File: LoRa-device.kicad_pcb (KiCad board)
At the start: 4 copper layers, 86.4 x 50.8 mm, 155 parts, among them J1 Micro_SD_Card_Det1, J3 Conn_01x04_Pin, J4 Conn_01x14_Pin, J6 Conn_01x04_Pin, J8 U.FL, P1 1_25T-1-2A, P2 1_25T-1-2A, SW1 EVQPUC02K, SW2 EVQPUC02K, U1 ESP32-S3, U11 MC-121-L119, U12 TLV62569DBV, U14 MCP23017_ML, U15 HJ-SMA275, U17 RA-01SH-P, U18 L76KB-A58, U19 MAX98357A, U2 W25Q128JVS, U4 STLQ015M33R, U5 SK-12D02-VG5, U6 USBLC6-2P6, U7 BQ25185DLHR, U8 TPS22917LDBV, Y1 32.768 kHz, Y2 40MHz(10ppm)

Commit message: Solved DRCs, updated case model
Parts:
- moved R11 8.22 mm to (112.4, 84.1)
- moved R40 5.28 mm to (131.0, 108.0), turned to 135 degrees
- moved G*** 3.70 mm to (148.6, 87.6)
- moved R39 2.53 mm to (134.8, 108.8), turned to 0 degrees
- moved C42 2.14 mm to (115.1, 112.3), turned to 90 degrees
- moved R14 2.10 mm to (141.6, 106.1), turned to 90 degrees
- moved R54 2.01 mm to (103.4, 121.6), turned to 180 degrees
- moved R24 1.68 mm to (109.5, 90.4)
- moved C4 1.38 mm to (137.4, 86.3)
- moved R23 1.38 mm to (136.3, 86.3)
- moved Y2 1.38 mm to (139.7, 86.3)
- moved C33 1.36 mm to (142.1, 85.7)
- moved D4 1.04 mm to (104.0, 123.1), turned to 0 degrees
- moved R13 0.95 mm to (108.1, 111.2), turned to 90 degrees
- moved R28 0.85 mm to (132.1, 96.3)
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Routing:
- net VDD_CPU: track 380.3 -> 390.4 mm, vias 46 -> 49
- net GPB5: track 70.4 -> 63.9 mm, vias 4 -> 6
- net SPIHD: track 0.00 -> 5.27 mm
- net Net-(U1-GPIO4): track 31.7 -> 27.7 mm
- net +5V: track 27.6 -> 24.8 mm
- net Net-(U1-XTAL_N): track 13.9 -> 11.7 mm
- net Net-(U1-GPIO1): track 28.7 -> 30.7 mm
- net Net-(J4-Pin_9): track 5.50 -> 7.21 mm
- net Net-(U1-XTAL_P): track 5.78 -> 4.45 mm
- net MTDO/IO40/I2C_SCK: track 41.5 -> 42.7 mm
- net GPA6: track 53.1 -> 54.2 mm
- net IO0: track 33.3 -> 34.4 mm
- net MISOB: track 55.2 -> 54.1 mm
- net IO1: track 58.1 -> 57.1 mm
- net MOSIB: track 70.5 -> 71.4 mm
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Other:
- board text removed: "BAT"

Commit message: Minor component changes.
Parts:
- removed C17: 10uF, Capacitor_SMD:C_0402_1005Metric
- removed C49: 10uF, PCM_JLCPCB:C_0402
- removed L7: 4.7uH 3V, Inductor_SMD:L_Sunlord_MWSA0402S
- removed MK1: SPH0645LM4H, Sensor_Audio:Knowles_SPH0645LM4H-6_3.5x2.65mm
- removed R39, R40: 33Ω, PCM_JLCPCB:R_0402
- added C21: 100nF, PCM_JLCPCB:C_0402, F.Cu at (154.2, 76.3)
- added U3: ICS-43432, LoRa_library:SENSOR-SMD_ICS-43432, F.Cu at (151.9, 76.5)
- added U9: MHCI04020-2R2M-R8, LoRa_library:IND-SMD_L4.6-W4.1, F.Cu at (113.0, 97.5)
- moved R43 47.4 mm to (150.9, 79.9), turned to -90 degrees
- moved R1 46.0 mm to (151.9, 79.9), turned to -90 degrees
- moved C56 16.3 mm to (115.4, 82.1), turned to 180 degrees
- moved C33 1.45 mm to (143.5, 85.7)
- moved C4 1.45 mm to (138.8, 86.3)
- moved R23 1.45 mm to (137.8, 86.3)
- moved Y2 1.45 mm to (141.1, 86.3)
- moved G*** 1.43 mm to (149.8, 88.4)
- moved C10 1.20 mm to (118.1, 88.3), turned to 90 degrees
- moved C13 1.13 mm to (129.2, 99.3)
- moved C32 1.13 mm to (129.2, 100.4)
- moved C39 0.61 mm to (134.8, 86.2)
- moved C40 0.61 mm to (134.8, 85.2)
- moved C37 0.25 mm to (114.4, 90.7)
- moved C38 0.25 mm to (114.4, 88.5)
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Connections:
- net Net-(U19-OUTN) renamed AUDIO_OUTN
- net Net-(U19-OUTP) renamed AUDIO_OUTP
- U1 pad 6: Net-(U1-GPIO1) -> IO1
- U1 pad 9: Net-(U1-GPIO4) -> IO4
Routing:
- net IO8: track 80.6 -> 28.6 mm
- net Net-(U1-GPIO1): track 30.7 -> 0.00 mm, vias 2 -> 0
- net Net-(U1-GPIO4): track 27.7 -> 0.00 mm, vias 2 -> 0
- net VDD_CPU: track 390.4 -> 370.1 mm, vias 49 -> 48
- net IO4: track 61.1 -> 58.1 mm, vias 2 -> 4
- net IO9/BAT: track 40.5 -> 43.2 mm
- net IO1: track 57.1 -> 54.5 mm
- net MOSIA: track 84.7 -> 82.1 mm
- net LORA_CS: track 59.6 -> 57.1 mm
- net GPA6: track 54.2 -> 52.2 mm
- net Net-(U1-XTAL_N): track 11.7 -> 13.2 mm
- net Net-(U1-XTAL_P): track 4.45 -> 5.90 mm
- net AUDIO_OUTP: track 9.30 -> 10.7 mm
- net GPA1: track 79.3 -> 77.9 mm
- net LORA_BUSY: track 47.9 -> 49.2 mm
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
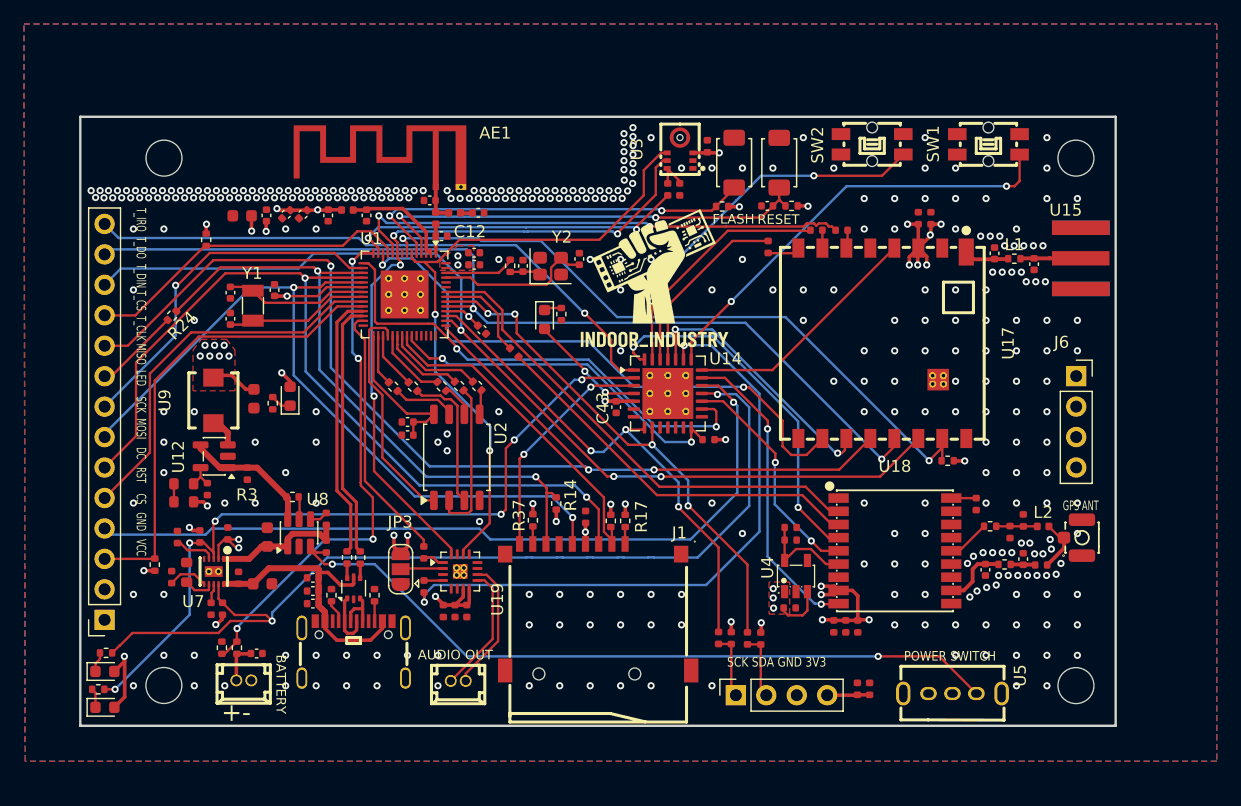
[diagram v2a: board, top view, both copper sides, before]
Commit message: Perfected 3V3 routing
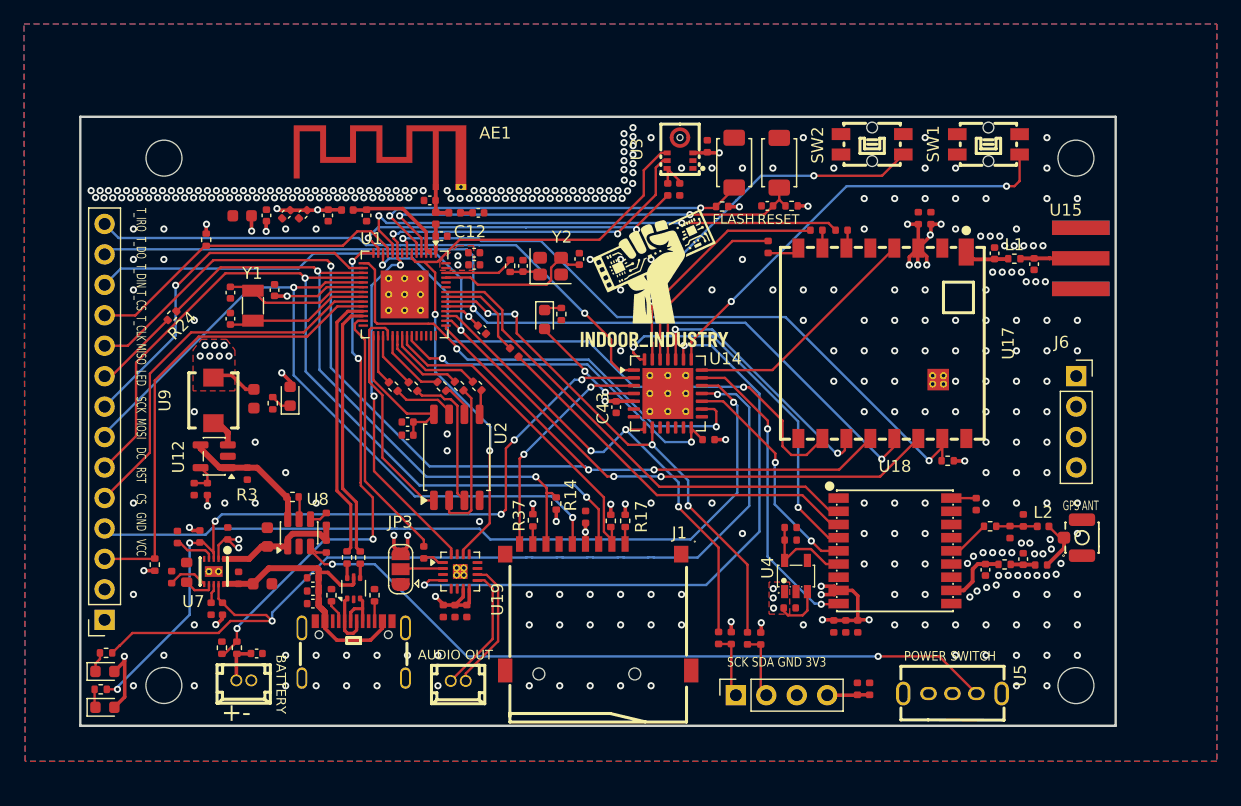
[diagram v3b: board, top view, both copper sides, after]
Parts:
- removed R50: 300kΩ, PCM_JLCPCB:R_0603
- removed R56: 150kΩ, PCM_JLCPCB:R_0603
- R38: value 2.2kΩ -> 22kΩ
- moved R38 20.8 mm to (111.4, 104.9), turned to -90 degrees
- moved R54 0.20 mm to (103.6, 121.6)
- turned R33 to 90 degrees
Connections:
- R33 pad 1: Net-(U12-FB) -> VDD_CPU
- R33 pad 2: GND -> Net-(U12-FB)
- R38 pad 1: GPA6 -> Net-(U12-FB)
- R38 pad 2: Net-(U19-~{SD_MODE}) -> GND
- U19 pad 4: Net-(U19-~{SD_MODE}) -> GPA6
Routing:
- net VDD_CPU: track 370.1 -> 550.7 mm
- net Net-(U19-~{SD_MODE}): track 1.61 -> 0.00 mm
- net Net-(R50-Pad2): track 1.50 -> 0.00 mm
- net GND: vias 330 -> 327
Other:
- board text added: "LoRa Rev-B PROTOYPE, NOT FOR RESALE NO REGULATORY APPROVAL USE AT OWN RISK EVALUATION ONLY DESIGNED BY INDOOR_INDUSTRY 04/2026"

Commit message: Production ready prototype
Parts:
- removed L1: 0R, Resistor_SMD:R_0402_1005Metric
- removed R55: 1K, Resistor_SMD:R_0402_1005Metric
- removed R6: 330Ω, PCM_JLCPCB:R_0402
- removed U4: STLQ015M33R, LoRa_library:SOT-23-5_L3.0-W1.7-P0.95-LS2.8-BR
- added C17: 1uF, PCM_JLCPCB:C_0402, F.Cu at (159.2, 81.3)
- added C34: 10uF, PCM_JLCPCB:C_0603, F.Cu at (119.5, 113.3)
- added C49: 12pF, PCM_JLCPCB:C_0402, F.Cu at (114.5, 88.5)
- added L4: 24nH, PCM_JLCPCB:L_0402, F.Cu at (136.9, 86.8)
- added R39: 10kΩ, PCM_JLCPCB:R_0402, F.Cu at (161.2, 81.3)
- added R40: 47kΩ, PCM_JLCPCB:R_0402, F.Cu at (114.5, 117.6)
- added R42: 5.1kΩ, PCM_JLCPCB:R_0402, F.Cu at (126.5, 113.7)
- added R50: 0Ω, PCM_JLCPCB:R_0402, F.Cu at (119.7, 105.7)
- added U10: XC6206P332MR, PCM_JLCPCB:SOT-23-3_L2.9-W1.6-P1.90-LS2.8-BR, F.Cu at (158.6, 108.2)
- C10, C15, C18, C32: value 0.1uF -> 100nF; footprint Capacitor_SMD:C_0402_1005Metric -> PCM_JLCPCB:C_0402
- C11: value 0.1uF -> 10uF; footprint Capacitor_SMD:C_0402_1005Metric -> PCM_JLCPCB:C_0402
- C12, C14, C26, C31, C37, C38, DNP2, DNP4, DNP6, DNP7: footprint Capacitor_SMD:C_0402_1005Metric -> PCM_JLCPCB:C_0402
- C13: value 1uF -> 10uF; footprint Capacitor_SMD:C_0402_1005Metric -> PCM_JLCPCB:C_0402
- C16, C3: value 10uF -> 100nF; footprint Capacitor_SMD:C_0402_1005Metric -> PCM_JLCPCB:C_0402
- C19: value 0.1uF -> 1uF; footprint Capacitor_SMD:C_0402_1005Metric -> PCM_JLCPCB:C_0402
- C22: value 0.1uF -> 12pF; footprint Capacitor_SMD:C_0402_1005Metric -> PCM_JLCPCB:C_0402
- C25: value 10uF -> 1uF; footprint Capacitor_SMD:C_0402_1005Metric -> PCM_JLCPCB:C_0402
- C33: value 12pF -> 100nF; footprint Capacitor_SMD:C_0402_1005Metric -> PCM_JLCPCB:C_0402
- C39: value 1uF -> 100nF; footprint Capacitor_SMD:C_0402_1005Metric -> PCM_JLCPCB:C_0402
- C4: value 12pF -> 10uF; footprint Capacitor_SMD:C_0402_1005Metric -> PCM_JLCPCB:C_0402
- C40: value 10nF -> 100nF; footprint Capacitor_SMD:C_0402_1005Metric -> PCM_JLCPCB:C_0402
- C43: value 0.1uF -> 4.7uF; footprint Capacitor_SMD:C_0402_1005Metric -> PCM_JLCPCB:C_0402
- C5: value 4.7uF -> 1uF
- C6: footprint Capacitor_SMD:C_0402_1005Metric -> PCM_JLCPCB:C_0603
- C8: value 10uF -> 10nF; footprint Capacitor_SMD:C_0402_1005Metric -> PCM_JLCPCB:C_0402
- C9: value 100nF -> 33pF
- J1: footprint my_footprints:TF-SMD_TF-01A -> LoRa_library:TF-SMD_TF-01A
- L2, L3, L5, L6: footprint Inductor_SMD:L_0402_1005Metric -> PCM_JLCPCB:L_0402
- R10, R21: value 10K -> 0Ω; footprint Resistor_SMD:R_0402_1005Metric -> PCM_JLCPCB:R_0402
- R11, R14, R17, R22, R31, R37: value 10K -> 10kΩ; footprint Resistor_SMD:R_0402_1005Metric -> PCM_JLCPCB:R_0402
- R12, R19: value 200K -> 470Ω; footprint Resistor_SMD:R_0402_1005Metric -> PCM_JLCPCB:R_0402
- R13: value 10K -> 5.1kΩ; footprint Resistor_SMD:R_0402_1005Metric -> PCM_JLCPCB:R_0402
- R16, R25: value 470R -> 10kΩ; footprint Resistor_SMD:R_0402_1005Metric -> PCM_JLCPCB:R_0402
- R18, R2: value 33R -> 1kΩ; footprint Resistor_SMD:R_0402_1005Metric -> PCM_JLCPCB:R_0402
- R23: value 0R -> 47kΩ; footprint Resistor_SMD:R_0402_1005Metric -> PCM_JLCPCB:R_0402
- R24, R36: value 0R -> 100Ω; footprint Resistor_SMD:R_0402_1005Metric -> PCM_JLCPCB:R_0402
- R26, R27, R28, R29, R30, R9: value 0R -> 0Ω; footprint Resistor_SMD:R_0402_1005Metric -> PCM_JLCPCB:R_0402
- R3: value 0R -> 10kΩ; footprint Resistor_SMD:R_0402_1005Metric -> PCM_JLCPCB:R_0402
- R34, R35: value 5.1K -> 33Ω; footprint Resistor_SMD:R_0402_1005Metric -> PCM_JLCPCB:R_0402
- R54: value 1K -> 0Ω; footprint Resistor_SMD:R_0402_1005Metric -> PCM_JLCPCB:R_0402
- moved R54 75.4 mm to (177.8, 108.0)
- moved R9 72.5 mm to (109.5, 90.4), turned to 45 degrees
- moved R11 64.6 mm to (174.3, 102.5), turned to 0 degrees
- moved R30 53.1 mm to (179.0, 111.2), turned to 0 degrees
- moved R36 42.4 mm to (138.4, 92.3), turned to -45 degrees
- moved R31 41.1 mm to (112.4, 84.1), turned to 90 degrees
- moved R23 39.9 mm to (114.5, 118.7), turned to 180 degrees
- moved R19 39.9 mm to (142.1, 90.2), turned to -90 degrees
- moved C8 38.0 mm to (134.8, 85.2)
- moved C40 37.1 mm to (162.2, 110.2), turned to -90 degrees
- moved C15 35.4 mm to (123.9, 84.2)
- moved R37 31.8 mm to (108.0, 111.2)
- moved R21 31.3 mm to (128.0, 96.3), turned to -45 degrees
- moved C38 29.2 mm to (143.4, 85.7), turned to 90 degrees
- moved R24 28.2 mm to (137.7, 93.1), turned to -45 degrees
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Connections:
- C10 pad 1: VDD_CPU -> GND
- C10 pad 2: GND -> Net-(C10-Pad2)
- C13 pad 1: VDD_SPI -> VBAT
- C15 pad 1: EN -> IO9/BAT
- C19 pad 1: Net-(C19-Pad1) -> VDD_CPU
- C22 pad 1: +5V -> XTAL32N
- C26 pad 1: VDD_CPU -> VDD_SPI
- C3 pad 1: VDD_CPU -> VDD_SPI
- C32 pad 1: VDD_SPI -> VDD_CPU
- C33 pad 2: Net-(U1-XTAL_N) -> VDD_CPU
- C37 pad 1: XTAL32N -> GND
- C37 pad 2: GND -> Net-(C37-Pad2)
- C38 pad 1: XTAL32P -> Net-(U1-XTAL_N)
- C39 pad 1: VDD_CPU -> GND
- C39 pad 2: GND -> VDD_CPU
- C4 pad 1: Net-(C4-Pad1) -> VDD_CPU
- C40 pad 1: VDD_CPU -> GND
- C40 pad 2: GND -> Net-(U10-VOUT)
- C43 pad 1: GND -> Net-(U10-VOUT)
- C43 pad 2: VDD_CPU -> GND
- C5 pad 1: Net-(U18-V_BCKP) -> Net-(U10-VOUT)
- C8 pad 1: VBAT -> VDD_CPU
- C9 pad 1: Net-(U18-V_BCKP) -> GND
- C9 pad 2: GND -> Net-(U10-VOUT)
- L3 pad 2: Net-(C19-Pad1) -> Net-(C10-Pad2)
- R10 pad 1: VDD_CPU -> Net-(U17-ANT)
- R10 pad 2: LORA_CS -> Net-(DNP4-Pad1)
- R11 pad 1: VDD_CPU -> LORA_CS
- R11 pad 2: TOUCH_CS -> VDD_CPU
- R12 pad 1: VBAT -> Net-(D2-K)
- R12 pad 2: IO9/BAT -> GND
- R13 pad 1: VDD_CPU -> Net-(U11-CC1)
- R13 pad 2: SCREEN_CS -> GND
- R14 pad 1: VDD_CPU -> MISOB
- R14 pad 2: MISOB -> VDD_CPU
- R16 pad 1: Net-(D2-K) -> VDD_CPU
- R16 pad 2: GND -> Net-(J1-DAT1)
- R17 pad 1: VDD_CPU -> SPICLK_N/IO48/SD_CS
- R17 pad 2: Net-(J1-DAT2) -> VDD_CPU
- R18 pad 1: Net-(R18-Pad1) -> Net-(D5-K)
- R18 pad 2: USB_D+ -> GPA1
- R19 pad 1: IO9/BAT -> Net-(D3-K)
- R2 pad 1: Net-(R2-Pad1) -> Net-(D4-K)
- R2 pad 2: USB_D- -> GPB5
- R21 pad 1: VDD_CPU -> Net-(U1-SPIHD)
- R21 pad 2: IO0 -> SPIHD
- R22 pad 1: EN -> VDD_CPU
- R22 pad 2: VDD_CPU -> IO0
- R23 pad 1: Net-(C4-Pad1) -> VBAT
- R23 pad 2: Net-(U1-XTAL_P) -> IO9/BAT
- R24 pad 1: MISOB -> Net-(U1-U0TXD)
- R24 pad 2: Net-(J4-Pin_9) -> GPS_RXD
- R25 pad 1: Net-(D3-K) -> VDD_CPU
- R25 pad 2: GND -> Net-(J1-DAT2)
- R26 pad 1: Net-(U1-SPID) -> Net-(U1-SPIWP)
- R26 pad 2: SPID -> SPIWP
- R27 pad 1: Net-(U1-SPIQ) -> Net-(U1-SPICLK)
- R27 pad 2: SPIQ -> SPISCK
- R28 pad 1: Net-(U1-SPICLK) -> Net-(U1-SPIQ)
- R28 pad 2: SPISCK -> SPIQ
- R29 pad 1: Net-(U1-SPIWP) -> Net-(U1-SPID)
- R29 pad 2: SPIWP -> SPID
- R3 pad 1: Net-(U8-QOD) -> VDD_SPI
- R3 pad 2: VSYS_SW -> SPICS0
- R30 pad 1: Net-(U1-SPIHD) -> Net-(U18-RF_IN)
- R30 pad 2: SPIHD -> Net-(C27-Pad1)
- R31 pad 1: VDD_CPU -> TOUCH_CS
- R31 pad 2: SPICLK_N/IO48/SD_CS -> VDD_CPU
- R34 pad 1: GND -> Net-(R34-Pad1)
- R34 pad 2: Net-(U11-CC1) -> USB_D-
- R35 pad 1: GND -> Net-(R35-Pad1)
- R35 pad 2: Net-(U11-CC2) -> USB_D+
- R36 pad 1: Net-(C28-Pad1) -> Net-(U1-U0RXD)
- R36 pad 2: Net-(U18-VDD_RF) -> GPS_TXD
- R37 pad 1: VDD_CPU -> SCREEN_CS
- R37 pad 2: Net-(J1-DAT1) -> VDD_CPU
- R47 pad 2: Net-(J3-Pin_2) -> MTMS/IO42/I2C_SDA
- R48 pad 2: Net-(J3-Pin_1) -> MTDO/IO40/I2C_SCK
- R54 pad 1: GPB5 -> Net-(C28-Pad1)
- R54 pad 2: Net-(D4-K) -> Net-(U18-VDD_RF)
- R9 pad 1: Net-(U18-RF_IN) -> Net-(J4-Pin_9)
- R9 pad 2: Net-(C27-Pad1) -> MISOB
- U1 pad 2: Net-(C19-Pad1) -> Net-(C10-Pad2)
- U1 pad 3: Net-(C19-Pad1) -> Net-(C10-Pad2)
- U1 pad 50: GPS_TXD -> Net-(U1-U0RXD)
- U18 pad 6: Net-(U18-V_BCKP) -> Net-(U10-VOUT)
- U6 pad 4: Net-(R18-Pad1) -> Net-(R35-Pad1)
- U6 pad 6: Net-(R2-Pad1) -> Net-(R34-Pad1)
- Y2 pad 1: Net-(C4-Pad1) -> Net-(C37-Pad2)
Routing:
- net VDD_CPU: track 550.7 -> 538.1 mm, vias 48 -> 45
- net Net-(C19-Pad1): track 8.85 -> 0.00 mm
- net Net-(C10-Pad2): track 0.00 -> 8.85 mm
- net GPS_TXD: track 41.3 -> 32.5 mm
- net Net-(U18-V_BCKP): track 8.16 -> 0.00 mm
- net Net-(U1-U0RXD): track 0.00 -> 7.75 mm
- net Net-(U10-VOUT): track 0.00 -> 7.35 mm
- net Net-(C37-Pad2): track 0.00 -> 3.00 mm
- net VBAT: track 69.2 -> 66.4 mm, vias 5 -> 3
- net GPA1: track 77.9 -> 75.1 mm
- net Net-(C4-Pad1): track 2.60 -> 0.00 mm
- net MTDO/IO40/I2C_SCK: track 42.7 -> 44.7 mm
- net MTMS/IO42/I2C_SDA: track 43.5 -> 45.4 mm
- net Net-(U1-XTAL_P): track 5.90 -> 4.06 mm
- net SPICS0: track 19.0 -> 20.7 mm
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- removed copper zone on F.Cu, net VBAT
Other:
- board text added: "Mercurio Rev-B PROTOYPE, NOT FOR RESALE NO REGULATORY APPROVAL USE AT OWN RISK EVALUATION ONLY DESIGNED BY INDOOR_INDUSTRY 04/2026"
- board text added: "VCC GND CS RST DC MOSI SCK LED MISO T_CLK T_CS T_DIN T_DO T_IRQ"
- board text removed: "LoRa Rev-B PROTOYPE, NOT FOR RESALE NO REGULATORY APPROVAL USE AT OWN RISK EVALUATION ONLY DESIGNED BY INDOOR_INDUSTRY 04/2026"

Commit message: Production ready prototype
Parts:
- added R55: 0Ω, PCM_JLCPCB:R_0402, F.Cu at (121.0, 88.0)
- added R56: 0Ω, PCM_JLCPCB:R_0402, F.Cu at (135.0, 94.1)
- added R57: 0Ω, PCM_JLCPCB:R_0402, F.Cu at (134.1, 92.2)
- added R58: 0Ω, PCM_JLCPCB:R_0402, F.Cu at (108.8, 84.9)
- added R59: 0Ω, PCM_JLCPCB:R_0402, F.Cu at (168.4, 102.4)
- added R6: 0Ω, PCM_JLCPCB:R_0402, F.Cu at (121.0, 87.2)
- added R60: 0Ω, PCM_JLCPCB:R_0402, F.Cu at (140.6, 107.5)
- added R61: 10kΩ, PCM_JLCPCB:R_0402, F.Cu at (138.9, 103.0)
- added R62: 10kΩ, PCM_JLCPCB:R_0402, F.Cu at (107.0, 106.5)
- added R63: 10kΩ, PCM_JLCPCB:R_0402, F.Cu at (169.8, 82.7)
- added R65: 0Ω, PCM_JLCPCB:R_0402, F.Cu at (141.1, 93.0)
- added R67: 10kΩ, PCM_JLCPCB:R_0402, F.Cu at (139.8, 89.9)
- added TP1: TestPoint, TestPoint:TestPoint_Loop_D1.80mm_Drill1.0mm_Beaded, F.Cu at (158.2, 92.7)
- moved D3 2.35 mm to (142.9, 91.1)
- moved R47 2.25 mm to (159.8, 117.4)
- moved R3 2.21 mm to (129.4, 104.1), turned to -90 degrees
- moved R17 2.05 mm to (146.1, 105.5), turned to 0 degrees
- moved R14 1.75 mm to (140.1, 105.3), turned to 180 degrees
- moved R49 1.48 mm to (111.0, 112.2)
- moved R51 0.97 mm to (109.8, 111.8)
- moved R43 0.91 mm to (150.8, 80.8)
- moved R1 0.85 mm to (151.3, 79.3), turned to 0 degrees
- moved C5 0.74 mm to (159.6, 111.2), turned to -90 degrees
- moved G*** 0.70 mm to (150.0, 87.8)
- moved C7 0.65 mm to (171.2, 82.7)
- moved C36 0.65 mm to (172.3, 82.7)
- moved R19 0.61 mm to (141.6, 90.5)
- moved R46 0.58 mm to (158.7, 84.8), turned to 0 degrees
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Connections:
- J1 pad 7: MISOB -> Net-(J1-DAT0)
- J4 pad 13: MISOA -> Net-(J4-Pin_13)
- U1 pad 18: MOSIB -> Net-(U1-GPIO13)
- U1 pad 19: SCKB -> Net-(U1-GPIO14)
- U1 pad 23: SCREEN_DC -> LORA_RST
- U1 pad 43: SCKA -> Net-(U1-GPIO38)
- U1 pad 44: MOSIA -> Net-(U1-MTCK)
- U1 pad 52: unconnected-(U1-GPIO46-Pad52) -> Net-(U1-GPIO46)
- U14 pad 21: LORA_RST -> Net-(U14-GPA4)
- U17 pad 13: MISOA -> Net-(U17-MISO)
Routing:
- net VDD_CPU: track 538.1 -> 454.1 mm, vias 45 -> 41
- net LORA_RST: track 20.3 -> 89.4 mm, vias 0 -> 2
- net SCREEN_DC: track 32.2 -> 51.0 mm, vias 0 -> 3
- net Net-(U1-GPIO46): track 0.00 -> 11.0 mm
- net VBAT: track 66.4 -> 76.4 mm, vias 3 -> 4
- net MISOA: track 79.4 -> 72.7 mm, vias 2 -> 3
- net Net-(U14-GPA4): track 0.00 -> 5.34 mm
- net Net-(J4-Pin_13): track 0.00 -> 4.60 mm
- net SCKB: track 64.8 -> 60.3 mm
- net SCKA: track 97.3 -> 92.8 mm
- net MOSIB: track 72.2 -> 67.8 mm
- net Net-(U1-GPIO14): track 0.00 -> 4.16 mm
- net Net-(U1-GPIO13): track 0.00 -> 4.05 mm
- net Net-(U1-GPIO38): track 0.00 -> 3.42 mm
- net SCREEN_RST: track 66.2 -> 69.4 mm
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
